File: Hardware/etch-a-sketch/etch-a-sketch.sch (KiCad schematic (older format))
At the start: 38 parts, among them J1 USART, J2 Conn_02x05_Odd_Even, J3 OLED, J4 Micro USB B, SW1 Encoder 1, SW2 Encoder 2, U1 AMS1117-3.3, U2 STM32F401RET6

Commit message: feat: route encoder buttons to NRST, add decoupling capacitor
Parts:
- C14: renamed from C?; footprint (none) -> Capacitor_SMD:C_0402_1005Metric
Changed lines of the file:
@@
 NRST
 $Comp
-L power:GND #PWR?
+L power:GND #PWR026
 U 1 1 5EB42673
 P 6400 4650
-F 0 "#PWR?" H 6400 4400 50  0001 C CNN
+F 0 "#PWR026" H 6400 4400 50  0001 C CNN
 F 1 "GND" H 6405 4477 50  0000 C CNN
 F 2 "" H 6400 4650 50  0001 C CNN
@@
 	6400 3750 6400 4250
 $Comp
-L Device:C_Small C?
+L Device:C_Small C14
 U 1 1 5EB51000
 P 6550 3850
-F 0 "C?" H 6642 3896 50  0000 L CNN
+F 0 "C14" H 6642 3896 50  0000 L CNN
 F 1 "100nF" H 6642 3805 50  0000 L CNN
-F 2 "" H 6550 3850 50  0001 C CNN
+F 2 "Capacitor_SMD:C_0402_1005Metric" H 6550 3850 50  0001 C CNN
 F 3 "~" H 6550 3850 50  0001 C CNN
 	1    6550 3850
@@
 $EndComp
 $Comp
-L power:GND #PWR?
+L power:GND #PWR027
 U 1 1 5EB7A007
 P 6550 3950
-F 0 "#PWR?" H 6550 3700 50  0001 C CNN
+F 0 "#PWR027" H 6550 3700 50  0001 C CNN
 F 1 "GND" H 6555 3777 50  0000 C CNN
 F 2 "" H 6550 3950 50  0001 C CNN

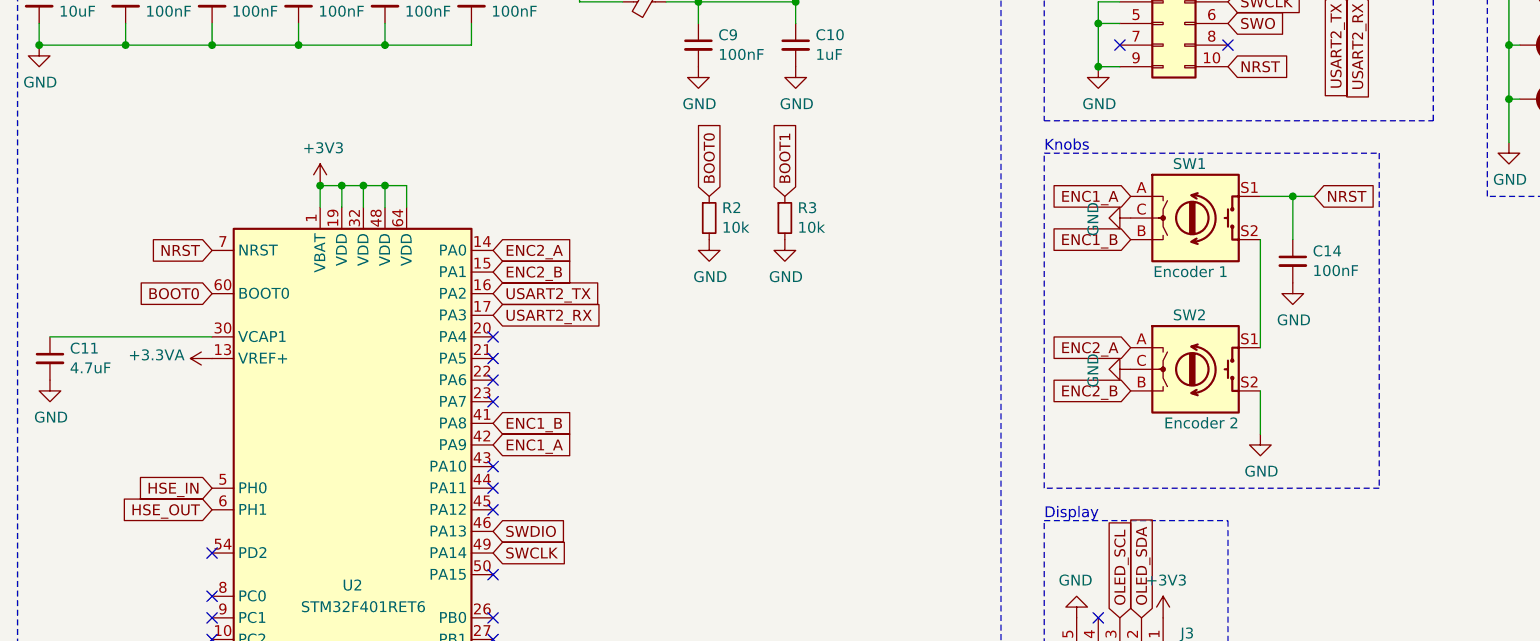
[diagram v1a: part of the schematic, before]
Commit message: refactor: move NRST decoupling capacitor close to MCU
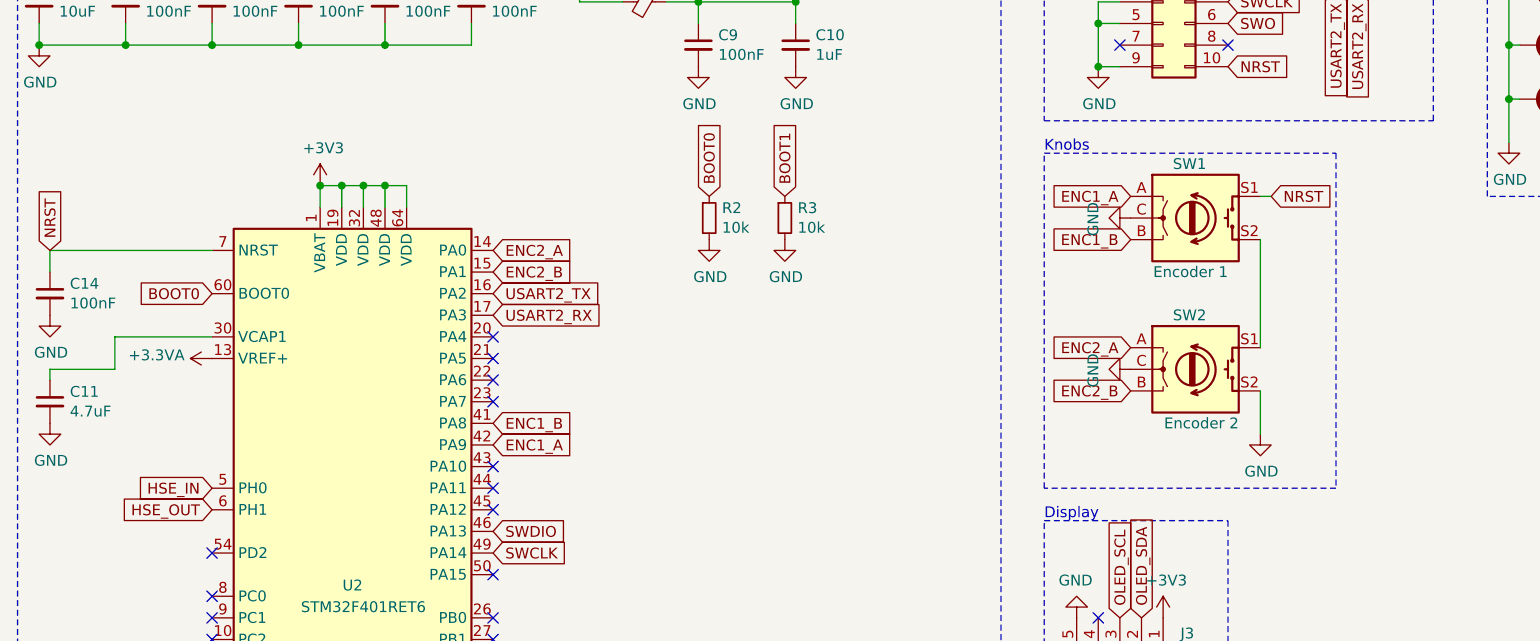
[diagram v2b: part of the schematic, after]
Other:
- moved on the sheet: C11, C14
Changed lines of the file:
@@
 $EndComp
 Connection ~ 750  2850
-Wire Wire Line
-	1550 4200 800  4200
 $Comp
 L power:GND #PWR018
 U 1 1 5EB90BA7
-P 800 4400
-F 0 "#PWR018" H 800 4150 50  0001 C CNN
-F 1 "GND" H 805 4227 50  0000 C CNN
-F 2 "" H 800 4400 50  0001 C CNN
-F 3 "" H 800 4400 50  0001 C CNN
-	1    800  4400
-	1    0    0    -1
-$EndComp
-Text GLabel 1550 3800 0    50   Input ~ 0
+P 800 4600
+F 0 "#PWR018" H 800 4350 50  0001 C CNN
+F 1 "GND" H 805 4427 50  0000 C CNN
+F 2 "" H 800 4600 50  0001 C CNN
+F 3 "" H 800 4600 50  0001 C CNN
+	1    800  4600
+	1    0    0    -1
+$EndComp
+Text GLabel 800  3800 1    50   Input ~ 0
 NRST
 Text GLabel 1550 4000 0    50   Input ~ 0
@@
 L Device:C_Small C11
 U 1 1 5EB7A09B
-P 800 4300
-F 0 "C11" H 892 4346 50  0000 L CNN
-F 1 "4.7uF" H 892 4255 50  0000 L CNN
-F 2 "Capacitor_SMD:C_0603_1608Metric" H 800 4300 50  0001 C CNN
-F 3 "~" H 800 4300 50  0001 C CNN
-	1    800  4300
+P 800 4500
+F 0 "C11" H 892 4546 50  0000 L CNN
+F 1 "4.7uF" H 892 4455 50  0000 L CNN
+F 2 "Capacitor_SMD:C_0603_1608Metric" H 800 4500 50  0001 C CNN
+F 3 "~" H 800 4500 50  0001 C CNN
+	1    800  4500
 	1    0    0    -1
 $EndComp
@@
 Debug
 Wire Notes Line
-	5400 3350 6950 3350
-Wire Notes Line
-	6950 3350 6950 4900
-Wire Notes Line
-	6950 4900 5400 4900
+	5400 3350 6750 3350
+Wire Notes Line
+	6750 3350 6750 4900
+Wire Notes Line
+	6750 4900 5400 4900
 Wire Notes Line
 	5400 4900 5400 3350
@@
 	1    0    0    -1
 $EndComp
-Text GLabel 6650 3550 2    50   Input ~ 0
+Text GLabel 6450 3550 2    50   Input ~ 0
 NRST
 $Comp
@@
 L Device:C_Small C14
 U 1 1 5EB51000
-P 6550 3850
-F 0 "C14" H 6642 3896 50  0000 L CNN
-F 1 "100nF" H 6642 3805 50  0000 L CNN
-F 2 "Capacitor_SMD:C_0402_1005Metric" H 6550 3850 50  0001 C CNN
-F 3 "~" H 6550 3850 50  0001 C CNN
-	1    6550 3850
+P 800 4000
+F 0 "C14" H 892 4046 50  0000 L CNN
+F 1 "100nF" H 892 3955 50  0000 L CNN
+F 2 "Capacitor_SMD:C_0402_1005Metric" H 800 4000 50  0001 C CNN
+F 3 "~" H 800 4000 50  0001 C CNN
+	1    800  4000
 	1    0    0    -1
 $EndComp
@@
 L power:GND #PWR027
 U 1 1 5EB7A007
-P 6550 3950
-F 0 "#PWR027" H 6550 3700 50  0001 C CNN
-F 1 "GND" H 6555 3777 50  0000 C CNN
-F 2 "" H 6550 3950 50  0001 C CNN
-F 3 "" H 6550 3950 50  0001 C CNN
-	1    6550 3950
-	1    0    0    -1
-$EndComp
-Wire Wire Line
-	6400 3550 6550 3550
-Wire Wire Line
-	6550 3550 6550 3750
-Connection ~ 6550 3550
-Wire Wire Line
-	6550 3550 6650 3550
+P 800 4100
+F 0 "#PWR027" H 800 3850 50  0001 C CNN
+F 1 "GND" H 805 3927 50  0000 C CNN
+F 2 "" H 800 4100 50  0001 C CNN
+F 3 "" H 800 4100 50  0001 C CNN
+	1    800  4100
+	1    0    0    -1
+$EndComp
 Wire Wire Line
 	6400 4450 6400 4650
+Wire Wire Line
+	6400 3550 6450 3550
+Wire Wire Line
+	1550 4200 1100 4200
+Wire Wire Line
+	1550 3800 800  3800
+Wire Wire Line
+	800  3800 800  3900
+Wire Wire Line
+	1100 4200 1100 4350
+Wire Wire Line
+	1100 4350 800  4350
+Wire Wire Line
+	800  4350 800  4400
 $EndSCHEMATC
